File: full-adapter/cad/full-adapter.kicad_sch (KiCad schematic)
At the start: 0 parts

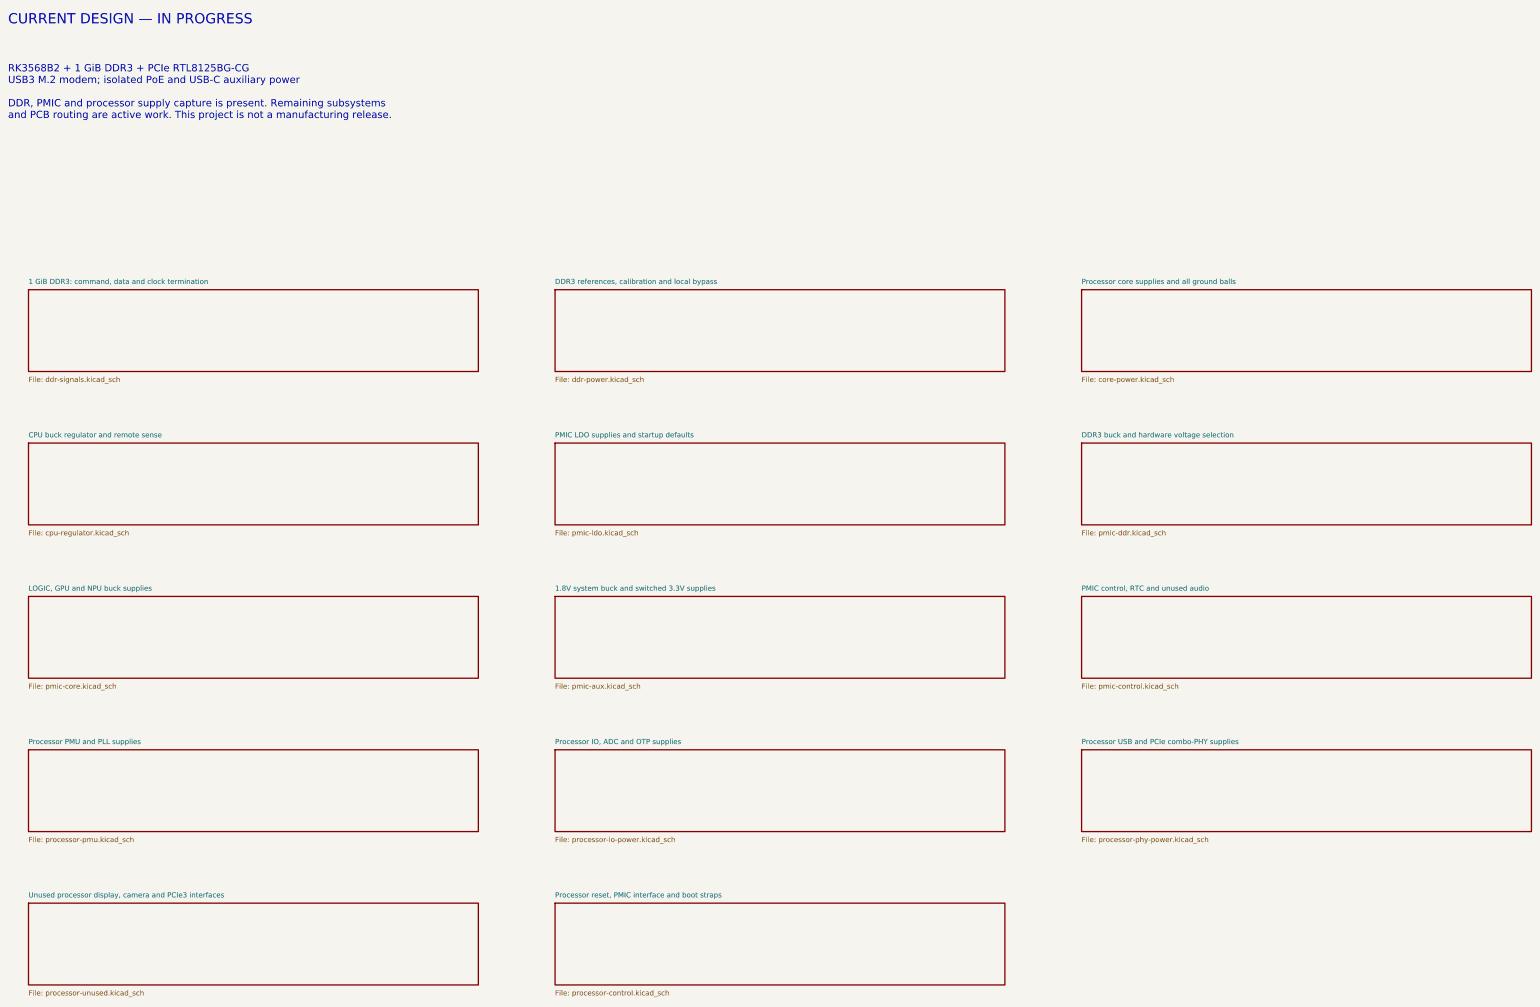
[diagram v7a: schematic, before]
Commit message: Capture processor 24 MHz oscillator and TVSS reference
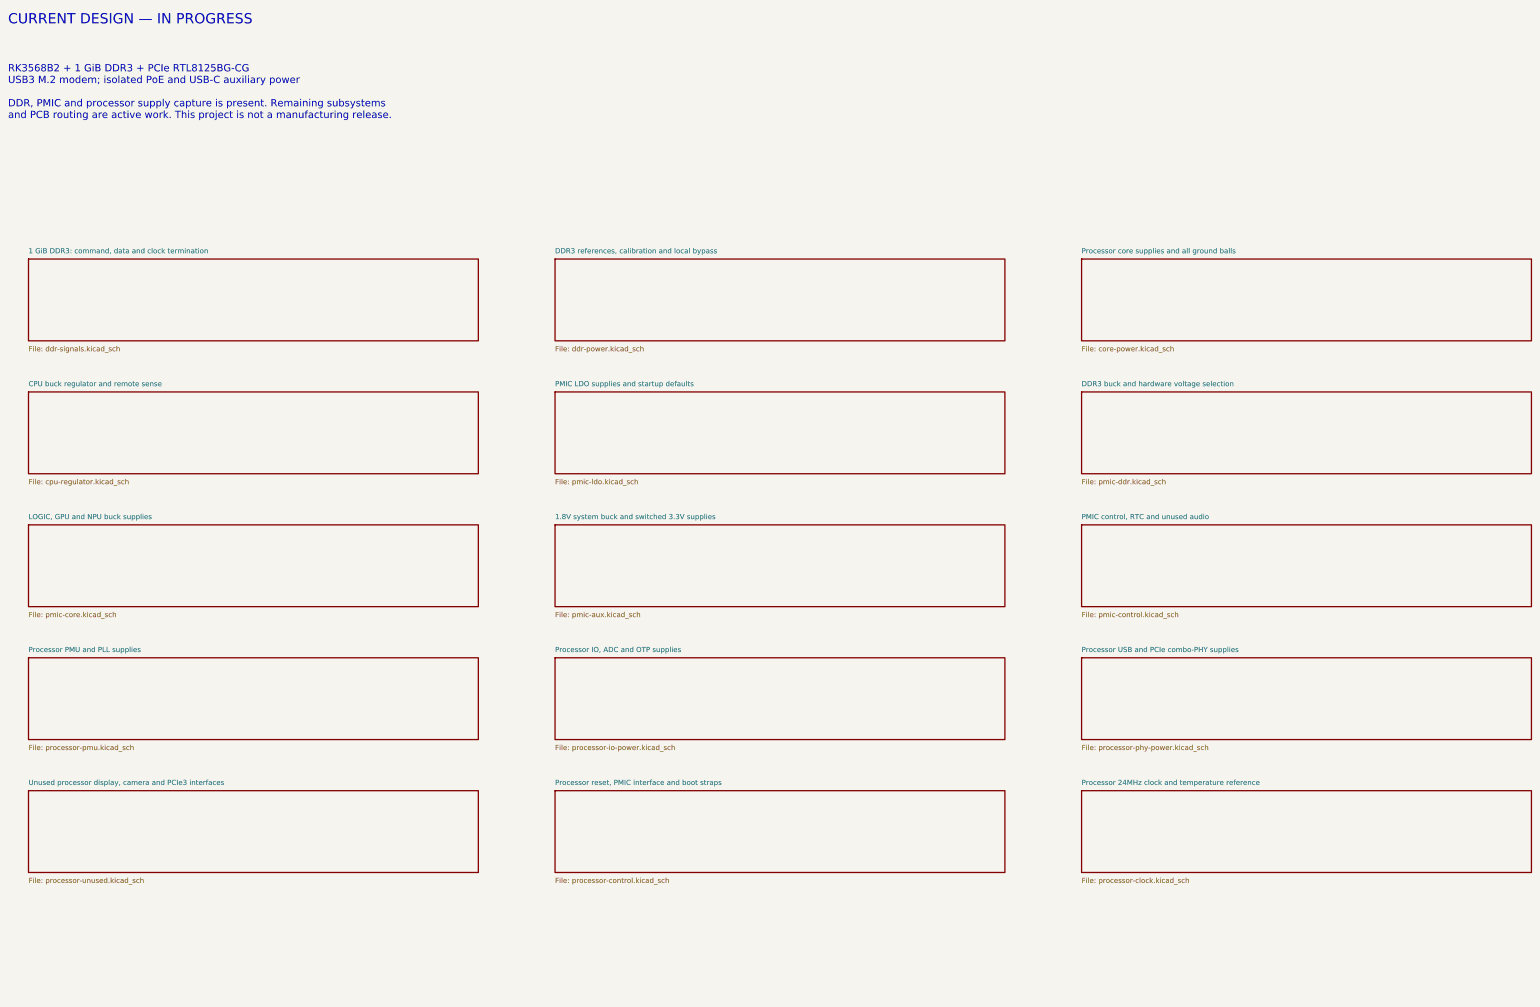
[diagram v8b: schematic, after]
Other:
- added sheet Processor 24MHz clock and temperature reference (processor-clock.kicad_sch)
